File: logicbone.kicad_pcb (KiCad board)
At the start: 8 copper layers, 86.4 x 54.6 mm, 278 parts, among them IC1 ECP5UM-CABGA381, IC10 W25Q128JVSIQ, IC11 FAN5362UMP, IC12 74LVC1G07, IC13 TPS51200, IC14 KSZ9031RNXCA, IC15 TC7USB40MU, IC16 NCP349, IC2 DDR3-TFBGA78, IC3 DDR3-TFBGA78, IC4 ACT8846QM460, IC5 PI6CG18401, IC6 74LVC1G02, IC7 FUSB302-QFN14, IC8 STM32FLxx-QFN48, IC9 ADC120, J1 NGFF-KEY-E, J2 GCT_USB4110_USBC, J3 ARJM11xx-502, J4 FTSH-105-DV-K, J5 Conn_02x05_Odd_Even, J6 Micro_SD_MEM2075, P8 BB_2x23, P9 BB_2x23, SW1 SW_SPST, SW2 SW_SPST, Y1 25MHz, Y2 32.768kHz

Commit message: Replace PMIC with MXL7704, switch to SPI master programming.
The Quorvo PMIC in the original design appears to have been deprecated
on DigiKey. Out of concern for availability, let's switch to the MXL7704
instead.

In an effort to support to an FPGA-based bootloader solution, we have
switched to using SPI master mode for the ECP5 configuration data. In
the long run this might allow a considerable downsizing of the STM32.
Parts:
- removed C168, C169, C172: 10uF, Capacitor_SMD:C_0603_1608Metric
- removed C470: 1nF, Capacitor_SMD:C_0402_1005Metric
- removed D1: LED_ARGB, KiCAD_Magic:LTST-C19HE1WT
- removed R10: 47k, Resistor_SMD:R_0402_1005Metric
- removed R14: 4.7k, Resistor_SMD:R_0402_1005Metric
- removed R15: 470, Resistor_SMD:R_0402_1005Metric
- removed R32, R33: 10k, Resistor_SMD:R_0402_1005Metric
- removed RN11: 4.7k, Resistor_SMD:R_Array_Concave_4x0603
- added FB1: MPZ1608S600, Inductor_SMD:L_0603_1608Metric, B.Cu at (157.6, 86.5)
- added IC17: NCP110AMX110, Package_DFN_QFN:UDFN-4-1EP_1x1mm_P0.65mm_EP0.48x0.48mm, F.Cu at (164.1, 66.8)
- added IC18: NCP110AMX110, Package_DFN_QFN:UDFN-4-1EP_1x1mm_P0.65mm_EP0.48x0.48mm, F.Cu at (156.6, 66.8)
- added IC19: NCP115AMX250, Package_DFN_QFN:UDFN-4-1EP_1x1mm_P0.65mm_EP0.48x0.48mm, F.Cu at (154.8, 64.8)
- added R34: 4.7k, Resistor_SMD:R_0402_1005Metric, F.Cu at (113.0, 87.5)
- C101, C102, C103, C107, C250, C255, C440, C468, C524, C529, FB8, FB9: moved to B.Cu
- C117: value 1nF -> 10uF; footprint Capacitor_SMD:C_0402_1005Metric -> Capacitor_SMD:C_0603_1608Metric; moved to B.Cu
- C465: value 0.1uF -> 100nF
- C467: value 0.1uF -> 100nF; moved to B.Cu
- IC10: value W25Q128JVSIQ -> AT25SL128A; footprint Package_DFN_QFN:DFN-8-1EP_6x5mm_P1.27mm_EP2x2mm -> Package_DFN_QFN:DFN-8-1EP_6x5mm_P1.27mm_EP4x4mm
- IC13: value TPS51200 -> TPS51206; footprint Package_SON:VSON-10-1EP_3x3mm_P0.5mm_EP1.65x2.4mm -> Logicbone:WSON-10EP-2x2mm
- IC4: value ACT8846QM460 -> MXL7704; footprint Package_DFN_QFN:QFN-48-1EP_6x6mm_P0.4mm_EP4.3x4.3mm -> Package_DFN_QFN:QFN-32-1EP_5x5mm_P0.5mm_EP3.65x3.65mm
- R1: value 27k -> 20
- R2: value 3.3k -> 20
- RN10: value 4.7k -> 10k; footprint Resistor_SMD:R_Array_Concave_4x0603 -> KiCAD_Magic:EXBD-1206
- moved C467 305.4 mm to (150.8, 104.0), turned to 90 degrees
- moved FB5 292.8 mm to (161.5, 66.5)
- moved C468 284.8 mm to (145.1, 82.3), turned to 90 degrees
- moved C250 282.2 mm to (161.5, 68.1)
- moved FB4 279.3 mm to (161.5, 68.1)
- moved C255 268.8 mm to (161.5, 66.5)
- moved FB9 256.0 mm to (126.4, 88.0)
- moved C400 249.5 mm to (126.4, 88.0), turned to 180 degrees
- moved C410 248.2 mm to (126.4, 86.4), turned to 180 degrees
- moved C103 197.3 mm to (161.9, 81.0), turned to 180 degrees
- moved C101 197.1 mm to (154.5, 81.0), turned to 90 degrees
- moved C164 195.3 mm to (165.9, 67.3), turned to 270 degrees
- moved C102 185.2 mm to (156.5, 72.0)
- moved C167 182.6 mm to (152.9, 63.6), turned to 90 degrees
- moved C165 177.7 mm to (158.4, 67.3), turned to 270 degrees
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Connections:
- C117 pad 1: VDDR -> VADC
- C117 pad 2: Net-(C117-Pad2) -> GND
- C118 pad 1: VCC -> VCC3V3
- C158 pad 1: VCC -> VCC3V3
- C159 pad 1: VCC -> VCC3V3
- C160 pad 1: VCC -> VCC3V3
- C161 pad 1: VCC -> VCC3V3
- C162 pad 1: VCCIOA -> VCC1V8
- C163 pad 1: VCCIOA -> VCC1V8
- C164 pad 1: VCCIOA -> VCC1V8
- C165 pad 1: VCCIOA -> VCC1V8
- C201 pad 1: VCC -> VCC3V3
- C202 pad 1: VCC -> VCC3V3
- C210 pad 1: VCC -> VCC3V3
- C211 pad 1: VCC -> VCC3V3
- C212 pad 1: VCC -> VCC3V3
- C220 pad 1: VCCIOA -> VCC3V3
- C221 pad 1: VCCIOA -> VCC3V3
- C222 pad 1: VCCIOA -> VCC3V3
- C230 pad 1: VCCIOB -> VCC1V8
- C231 pad 1: VCCIOB -> VCC1V8
- C232 pad 1: VCCIOB -> VCC1V8
- C300 pad 1: VCC -> VCC3V3
- C301 pad 1: VCC -> VCC3V3
- C302 pad 1: VCC -> VCC3V3
- C303 pad 1: VCC -> VCC3V3
- C304 pad 1: VCC -> VCC3V3
- C305 pad 1: VCC -> VCC3V3
- C306 pad 1: VCC -> VCC3V3
- C307 pad 1: VCC -> VCC3V3
- C462 pad 1: VDDR -> GND
- C464 pad 1: VDDR -> /FPGA Memory/DDR3_VREF
- C464 pad 2: /FPGA Memory/DDR3_VREF -> GND
- D7 pad 1: GND -> Net-(D7-Pad1)
- D7 pad 2: Net-(D7-Pad2) -> VCC1V8
- D8 pad 1: GND -> Net-(D8-Pad1)
- D8 pad 2: Net-(D8-Pad2) -> VCC1V8
- IC1 pad B12: /Ethernet/FPGA_USB+ -> Net-(IC1-PadB12)
- IC1 pad C12: /Ethernet/FPGA_USB- -> Net-(IC1-PadC12)
- IC1 pad F10: VCC -> VCC3V3
- IC1 pad F11: VCC -> VCC3V3
- IC1 pad F12: VCC -> VCC3V3
- IC1 pad F9: VCC -> VCC3V3
- IC1 pad H14: VCCIOA -> VCC3V3
- IC1 pad H15: VCCIOA -> VCC3V3
- IC1 pad J15: VCCIOA -> VCC3V3
- IC1 pad L14: VCCIOB -> VCC1V8
- IC1 pad L15: VCCIOB -> VCC1V8
- IC1 pad M15: VCCIOB -> VCC1V8
- IC1 pad N17: /FPGA SERDES/M2_SDIO_CLK -> /FPGA SERDES/M2_COEX2
- IC1 pad P18: /FPGA SERDES/M2_COEX2 -> /FPGA SERDES/M2_COEX1
- IC1 pad R16: /FPGA SERDES/M2_RXD -> /FPGA SERDES/M2_TXD
- IC1 pad R17: /FPGA SERDES/M2_TXD -> /FPGA SERDES/M2_RXD
- IC1 pad R2: Net-(IC1-PadR2) -> /Supervisor/~FLASH_CSEL
- IC1 pad R3: Net-(IC1-PadR3) -> /Supervisor/USB_SEL
- IC1 pad R4: Net-(IC1-PadR4) -> GND
- IC1 pad T17: /FPGA SERDES/M2_COEX1 -> /FPGA SERDES/M2_SDIO_CLK
- IC1 pad T2: /Supervisor/~FPGA_CSEL -> /Exp Headers/PWR_BUTTON
- IC1 pad T4: Net-(IC1-PadR4) -> +3V3
- IC1 pad U17: /FPGA SERDES/M2_USB_DM -> /FPGA SERDES/M2_LED1
- IC1 pad U18: /FPGA SERDES/M2_USB_DP -> /FPGA SERDES/M2_LED2
- IC1 pad U2: /Supervisor/~FPGA_HOLDN -> /Supervisor/FPGA_UART_TXD
- IC1 pad U3: /Supervisor/FPGA_SCLK -> /Supervisor/FLASH_SCLK
- IC1 pad U4: Net-(IC1-PadU4) -> GND
- IC1 pad V1: /Supervisor/FPGA_UART_TXD -> /Supervisor/FPGA_UART_CLK
- IC1 pad V2: /Supervisor/FPGA_MISO -> /Supervisor/FLASH_MISO
- IC1 pad W1: /Supervisor/FPGA_UART_CLK -> /Supervisor/FLASH_D3
- IC1 pad W2: /Supervisor/FPGA_MOSI -> /Supervisor/FLASH_MOSI
- IC1 pad Y2: Net-(IC1-PadY2) -> /Supervisor/FLASH_D2
- IC10 pad 2: /Supervisor/FLASH_D1 -> /Supervisor/FLASH_MISO
- IC10 pad 5: /Supervisor/FLASH_D0 -> /Supervisor/FLASH_MOSI
- IC12 pad 5: VCC -> VCC3V3
- IC13 pad 1: Net-(C470-Pad2) -> VDDR
- IC13 pad 10: VCC -> VCC3V3
- IC14 pad 1: VCC -> VCC3V3
- IC14 pad 12: VCC -> VCC3V3
- IC14 pad 16: VCC -> VCC3V3
- IC14 pad 34: VCC -> VCC3V3
- IC14 pad 40: VCC -> VCC3V3
- IC4 pad 1: Net-(IC4-Pad1) -> +3V3
- IC4 pad 12: Net-(IC4-Pad11) -> VBUS
- IC4 pad 14: VBUS -> Net-(IC4-Pad14)
- IC4 pad 15: VCC -> Net-(IC4-Pad14)
- IC4 pad 16: /Supervisor/PMIC_ENABLE -> Net-(IC4-Pad14)
- IC4 pad 17: Net-(C107-Pad1) -> GND
- IC4 pad 18: VBUS -> GND
- IC4 pad 19: Net-(IC4-Pad19) -> VCORE
- IC4 pad 2: Net-(IC4-Pad1) -> /Supervisor/PMIC_SDA
- IC4 pad 20: GND -> Net-(IC4-Pad20)
- IC4 pad 21: VCCIOA -> Net-(IC4-Pad21)
- IC4 pad 22: VADC -> Net-(IC4-Pad22)
- IC4 pad 23: /Supervisor/PMIC_SCL -> GND
- IC4 pad 24: /Supervisor/PMIC_SDA -> Net-(C107-Pad1)
- IC4 pad 25: VBUS -> VCC3V3
- IC4 pad 26: Net-(IC4-Pad26) -> GND
- IC4 pad 27: GND -> Net-(IC4-Pad27)
- IC4 pad 28: Net-(IC4-Pad28) -> VBUS
- IC4 pad 29: Net-(C117-Pad2) -> VBUS
- IC4 pad 3: GND -> /Supervisor/PMIC_SCL
- IC4 pad 30: VBUS -> Net-(IC4-Pad30)
- IC4 pad 31: /Supervisor/~PMIC_PBIN -> Net-(C107-Pad1)
- IC4 pad 32: /Supervisor/PMIC_PWRHOLD -> VDDR
- IC4 pad 33: /Ethernet/~SYS_RESET -> GND
- IC4 pad 4: VCCTRX -> /Supervisor/PMIC_SEQ
- IC4 pad 5: VCCIOB -> /Ethernet/~SYS_RESET
- IC4 pad 6: +3V3 -> /Supervisor/PMIC_ENABLE
- IC4 pad 7: VCCTRXA -> +3V3
- IC4 pad 8: /Supervisor/PMIC_VSELR2 -> VCCAUX
- IC4 pad 9: /Supervisor/~PMIC_PBSTAT -> VCC1V8
- IC5 pad 16: VCCIOB -> VCC1V8
- IC5 pad 21: VCCIOB -> VCC1V8
- IC5 pad 25: VCCIOB -> VCC1V8
- IC5 pad 31: VCCIOB -> VCC1V8
- IC5 pad 4: VCCIOB -> VCC1V8
- IC5 pad 5: VCC -> VCC3V3
- IC5 pad 9: VCCIOB -> VCC1V8
- IC8 pad 10: /Supervisor/~USB_INT -> /Supervisor/PMIC_ENABLE
- IC8 pad 12: /Supervisor/~FLASH_CSEL -> Net-(IC8-Pad12)
- IC8 pad 13: /Supervisor/FLASH_SCLK -> Net-(IC8-Pad13)
- IC8 pad 14: /Supervisor/PMIC_PWRHOLD -> /Supervisor/PMIC_SEQ
- IC8 pad 15: /Supervisor/PMIC_VSELR2 -> /FPGA Power/PWR_SERDES
- IC8 pad 16: /Supervisor/FLASH_D3 -> Net-(IC8-Pad16)
- IC8 pad 17: /Supervisor/FLASH_D2 -> Net-(IC8-Pad17)
- IC8 pad 18: /Supervisor/FLASH_D1 -> Net-(IC8-Pad18)
- IC8 pad 19: /Supervisor/FLASH_D0 -> Net-(IC8-Pad19)
- IC8 pad 2: /Supervisor/~PMIC_INT -> Net-(IC8-Pad2)
- IC8 pad 25: /Supervisor/~FPGA_CSEL -> /Supervisor/~FLASH_CSEL
- IC8 pad 26: /Supervisor/FPGA_SCLK -> /Supervisor/FLASH_SCLK
- IC8 pad 27: /Supervisor/FPGA_MISO -> /Supervisor/FLASH_MISO
- IC8 pad 28: /Supervisor/FPGA_MOSI -> /Supervisor/FLASH_MOSI
- IC8 pad 38: /Supervisor/~FPGA_HOLDN -> /Supervisor/~USB_INT
- IC9 pad 13: VCC -> VCC3V3
- J1 pad 2: VCC -> VCC3V3
- J1 pad 4: VCC -> VCC3V3
- J1 pad 72: VCC -> VCC3V3
- J1 pad 74: VCC -> VCC3V3
- J6 pad 4: VCC -> VCC3V3
- L1 pad 1: Net-(IC4-Pad26) -> Net-(IC4-Pad27)
- L1 pad 2: VCCIOA -> VCC3V3
- L2 pad 1: Net-(IC4-Pad1) -> Net-(IC4-Pad14)
- L3 pad 2: VCC -> VCC1V8
- L4 pad 1: Net-(IC4-Pad28) -> Net-(IC4-Pad30)
- P9 pad 3: VCC -> VCC3V3
- P9 pad 4: VCC -> VCC3V3
- R1 pad 1: GND -> Net-(IC1-PadB12)
- R1 pad 2: Net-(C117-Pad2) -> /Ethernet/FPGA_USB+
- R11 pad 1: /FPGA SERDES/M2_LED1 -> Net-(D7-Pad1)
- R11 pad 2: Net-(D7-Pad2) -> /FPGA SERDES/M2_LED1
- R12 pad 1: /FPGA SERDES/M2_LED2 -> Net-(D8-Pad1)
- R12 pad 2: Net-(D8-Pad2) -> /FPGA SERDES/M2_LED2
- R13 pad 1: VCC -> VCC3V3
- R16 pad 1: VCC -> VCC3V3
- R17 pad 1: VCC -> VCC3V3
- R18 pad 1: VCC -> VCC3V3
- R19 pad 1: VCC -> VCC3V3
- R2 pad 1: VDDR -> Net-(IC1-PadC12)
- R2 pad 2: Net-(C117-Pad2) -> /Ethernet/FPGA_USB-
- R20 pad 1: VCC -> VCC3V3
- R21 pad 1: VCC -> VCC3V3
- R26 pad 1: /Ethernet/FPGA_USB+ -> Net-(IC1-PadB12)
- R27 pad 1: VCC -> VCC3V3
- R28 pad 1: VCC -> VCC3V3
- R30 pad 2: VCC -> VCC3V3
- R31 pad 2: VCC -> VCC3V3
- R8 pad 1: VCCIOB -> VCC1V8
- RN10 pad 1: /Ethernet/MMC_DAT2 -> VCC3V3
- RN10 pad 2: /Ethernet/MMC_DAT3 -> Net-(RN10-Pad2)
- RN10 pad 4: Net-(RN10-Pad4) -> /Ethernet/MMC_DAT3
- RN10 pad 5: VCC -> /Ethernet/MMC_DAT2
- RN10 pad 6: VCC -> /Ethernet/MMC_CLK
- RN10 pad 7: VCC -> /Ethernet/MMC_DAT0
- RN10 pad 8: VCC -> /Ethernet/MMC_DAT1
- RN4 pad 5: VCCIOB -> VCC1V8
- RN4 pad 6: VCCIOB -> VCC1V8
- RN4 pad 7: VCCIOB -> VCC1V8
- RN4 pad 8: VCCIOB -> VCC1V8
- RN5 pad 3: /Supervisor/~FPGA_CSEL -> Net-(RN5-Pad3)
- RN5 pad 4: /Supervisor/~FPGA_HOLDN -> Net-(RN5-Pad4)
- RN7 pad 1: /Supervisor/~PMIC_PBSTAT -> /Supervisor/FLASH_D3
- RN7 pad 2: /Supervisor/PMIC_ENABLE -> Net-(RN7-Pad2)
- RN7 pad 3: /Supervisor/PMIC_VSELR2 -> /Supervisor/~FLASH_CSEL
- RN7 pad 4: /Supervisor/PMIC_PWRHOLD -> /Supervisor/FLASH_D2
- RN7 pad 5: VCC -> +3V3
- RN7 pad 6: GND -> +3V3
- RN8 pad 1: /Ethernet/~SYS_RESET -> /Supervisor/PMIC_SDA
- RN8 pad 3: /Supervisor/PMIC_SDA -> /Ethernet/~SYS_RESET
- RN8 pad 4: /Supervisor/~PMIC_INT -> /Supervisor/PMIC_SEQ
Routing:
- net VCC3V3: track 0.00 -> 241.3 mm, vias 0 -> 17
- net +3V3: track 27.6 -> 197.9 mm, vias 11 -> 14
- net VCC1V8: track 0.00 -> 162.6 mm, vias 0 -> 14
- net /FPGA Memory/DDR3_VREF: track 10.1 -> 137.4 mm, vias 5 -> 7
- net VCORE: track 31.1 -> 134.4 mm
- net /DDR3 Power/VDDR_CORE: track 25.5 -> 122.2 mm, vias 17 -> 18
- net GND: track 359.9 -> 446.4 mm, vias 114 -> 126
- net /Supervisor/~PMIC_INT: track 66.3 -> 0.00 mm, vias 2 -> 0
- net /Supervisor/USB_SEL: track 0.00 -> 65.1 mm, vias 0 -> 2
- net VDDR: track 17.5 -> 79.8 mm, vias 8 -> 9
- net /Supervisor/PMIC_ENABLE: track 1.05 -> 60.8 mm, vias 1 -> 2
- net /Supervisor/PMIC_SEQ: track 0.00 -> 57.8 mm, vias 0 -> 2
- net /Supervisor/PMIC_PWRHOLD: track 54.3 -> 0.00 mm, vias 2 -> 0
- net VCCAUX: track 6.30 -> 55.7 mm
- net VCC: track 46.4 -> 0.00 mm, vias 13 -> 0
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
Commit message: Add dedicated LDO for VCCAUX, and a bunch of cleanup
The MXL7704 is almost capable of booting the entire ECP5 on its own
without any help from the supervisor. So we would like to test it out
on the prototype boards. To accompish this, we need to use a dedicated
LDO for VCCAUX.

With that, I am rapidly running out of major work to do and from here
on out it's just going to be review and minor tweaks.
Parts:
- removed C153, C157, C251, C256, C263, C273: 10uF, Capacitor_SMD:C_0603_1608Metric
- removed C503: 100nF, Capacitor_SMD:C_0402_1005Metric
- removed C507: 10nF, Capacitor_SMD:C_0402_1005Metric
- removed FB6: MPZ1608S600, Inductor_SMD:L_0603_1608Metric
- removed RN12: 47, Resistor_SMD:R_Array_Concave_4x0402
- removed RN6: 470, Resistor_SMD:R_Array_Concave_4x0603
- added C120: 100nF, Capacitor_SMD:C_0402_1005Metric, B.Cu at (181.8, 67.0)
- added C121: 100nF, Capacitor_SMD:C_0402_1005Metric, B.Cu at (177.8, 67.0)
- added C122: 100nF, Capacitor_SMD:C_0402_1005Metric, B.Cu at (179.5, 66.8)
- added C123: 100nF, Capacitor_SMD:C_0402_1005Metric, B.Cu at (178.0, 72.2)
- added D1: LED_ALT, LED_SMD:LED_0603_1608Metric, F.Cu at (183.1, 86.2)
- added D6: D_Schottky_ALT, Diode_SMD:D_SOD-123F, F.Cu at (126.0, 92.4)
- added D9: LED_ALT, LED_SMD:LED_0603_1608Metric, F.Cu at (183.1, 88.0)
- added IC20: NCP115AMX250, Package_DFN_QFN:UDFN-4-1EP_1x1mm_P0.65mm_EP0.48x0.48mm, F.Cu at (128.6, 68.9)
- added Q1: Q_PMOS_GSD, Package_TO_SOT_SMD:SOT-23, F.Cu at (119.0, 56.0)
- added R10: 470, Resistor_SMD:R_0402_1005Metric, F.Cu at (178.2, 86.8)
- added R14: 47, Resistor_SMD:R_0402_1005Metric, B.Cu at (145.9, 84.3)
- added R15: 47, Resistor_SMD:R_0402_1005Metric, B.Cu at (154.4, 83.9)
- added RN11: 10k, Resistor_SMD:R_Array_Concave_4x0603, B.Cu at (133.5, 59.9)
- C104, C155, C156, C161, C304, C442, C443, C447, C460, R1, R2, R20, R21, R22, R23, R6: moved to B.Cu
- C117, C220, C254, C262, C264, C265, C266, C270, C271, C272, C280, C302, C430, C462, C467, C521: moved to F.Cu
- C469: value 0.1uF -> 100nF
- H5: value MountingHole -> MountingHole_Pad
- R16: value 10k -> 47; moved to B.Cu
- R17: value 10k -> 470
- R19: value 10k -> 4.7k
- Y2: footprint KiCAD_Magic:Crystal_4SMD_7x1.5mm -> Crystal:Crystal_SMD_3215-2Pin_3.2x1.5mm
- moved C201 335.9 mm to (161.0, 41.3)
- moved C454 315.9 mm to (134.4, 26.3)
- moved C456 312.9 mm to (131.5, 26.3)
- moved C446 311.3 mm to (134.4, 30.3)
- moved C455 309.3 mm to (131.5, 28.3)
- moved C452 309.2 mm to (134.4, 28.3)
- moved C451 306.3 mm to (137.3, 26.3)
- moved C453 305.0 mm to (131.5, 30.3)
- moved C450 303.3 mm to (131.5, 32.3)
- moved R6 299.3 mm to (181.8, 71.7), turned to 180 degrees
- moved C444 298.5 mm to (150.5, 26.6)
- moved C447 294.8 mm to (140.8, 104.6), turned to 90 degrees
- moved C412 294.1 mm to (156.9, 26.3)
- moved C445 286.2 mm to (150.5, 29.1)
- moved C420 284.9 mm to (155.0, 85.1)
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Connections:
- C108 pad 2: Net-(C108-Pad2) -> GND
- C109 pad 2: Net-(C108-Pad2) -> GND
- C162 pad 1: VCC1V8 -> VCC3V3
- FB7 pad 2: VCORE -> /Ethernet/ETH_1V2
- H5 pad 1: (no net) -> GND
- IC1 pad N1: Net-(IC1-PadN1) -> /FPGA Memory/~DDR3_RST
- IC1 pad N4: /FPGA Memory/~DDR3_RST -> Net-(IC1-PadN4)
- IC14 pad 43: Net-(IC14-Pad43) -> /Ethernet/ETH_LDO
- IC17 pad 3: /FPGA Power/PWR_SERDES -> VCC1V8
- IC18 pad 3: /FPGA Power/PWR_SERDES -> VCC1V8
- IC4 pad 20: Net-(IC4-Pad20) -> /Supervisor/PMIC_PGOOD
- IC4 pad 5: /Ethernet/~SYS_RESET -> /FPGA Power/PWR_VCCAUX
- IC4 pad 8: VCCAUX -> Net-(IC4-Pad8)
- IC5 pad 1: Net-(C108-Pad2) -> GND
- IC8 pad 14: /Supervisor/PMIC_SEQ -> Net-(IC8-Pad14)
- IC8 pad 18: Net-(IC8-Pad18) -> /Supervisor/PMIC_SEQ
- IC8 pad 19: Net-(IC8-Pad19) -> /Supervisor/PMIC_PGOOD
- P8 pad 3: VCCIOA -> Net-(P8-Pad3)
- P8 pad 4: VCCIOA -> Net-(P8-Pad4)
- P8 pad 5: VCCIOA -> Net-(P8-Pad5)
- P8 pad 6: VCCIOA -> Net-(P8-Pad6)
- R16 pad 1: VCC3V3 -> /FPGA Memory/DDR3_CK-
- R16 pad 2: /Ethernet/ETH_RXD3 -> Net-(C469-Pad1)
- R17 pad 1: VCC3V3 -> /Supervisor/FPGA_DONE
- R17 pad 2: /Ethernet/ETH_RXD2 -> +3V3
- R18 pad 1: VCC3V3 -> /FPGA Power/PWR_VCCAUX
- R18 pad 2: /Ethernet/ETH_RXD1 -> +3V3
- R19 pad 1: VCC3V3 -> +3V3
- R19 pad 2: /Ethernet/ETH_RXD0 -> /Ethernet/~SYS_RESET
- RN5 pad 1: /Exp Headers/SDA -> /Exp Headers/SCL
- RN5 pad 2: /Exp Headers/SCL -> /Exp Headers/SDA
- RN8 pad 3: /Ethernet/~SYS_RESET -> /Supervisor/PMIC_PGOOD
- Y1 pad 2: Net-(C108-Pad2) -> GND
- Y1 pad 4: Net-(C108-Pad2) -> GND
- Y2 pad 2: GND -> Net-(C106-Pad1)
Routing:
- net GND: track 446.4 -> 1270.2 mm, vias 126 -> 144
- net VCC3V3: track 241.3 -> 366.8 mm, vias 17 -> 21
- net /Supervisor/PMIC_PGOOD: track 0.00 -> 52.3 mm, vias 0 -> 3
- net /Exp Headers/PWR_BUTTON: track 76.2 -> 125.4 mm, vias 2 -> 3
- net +3V3: track 197.9 -> 243.0 mm, vias 14 -> 18
- net /FPGA Memory/DDR3_VREF: track 137.4 -> 103.9 mm
- net /Supervisor/FPGA_DONE: track 9.68 -> 43.2 mm, vias 0 -> 2
- net /Ethernet/ETH_1V2: track 17.1 -> 49.1 mm, vias 6 -> 7
- net Net-(J3-PadL1): track 0.00 -> 27.4 mm, vias 0 -> 1
- net /FPGA Memory/~DDR3_RST: track 12.6 -> 37.4 mm, vias 2 -> 3
- net /Supervisor/~FPGA_INIT: track 16.4 -> 38.4 mm, vias 2 -> 3
- net /Ethernet/ETH_LED_L: track 26.6 -> 47.8 mm
- net /FPGA Power/PWR_VCCAUX: track 0.00 -> 20.7 mm
- net /FPGA Power/PWR_SERDES: track 0.00 -> 19.8 mm, vias 0 -> 2
- net VCCIOA: track 18.4 -> 0.00 mm
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
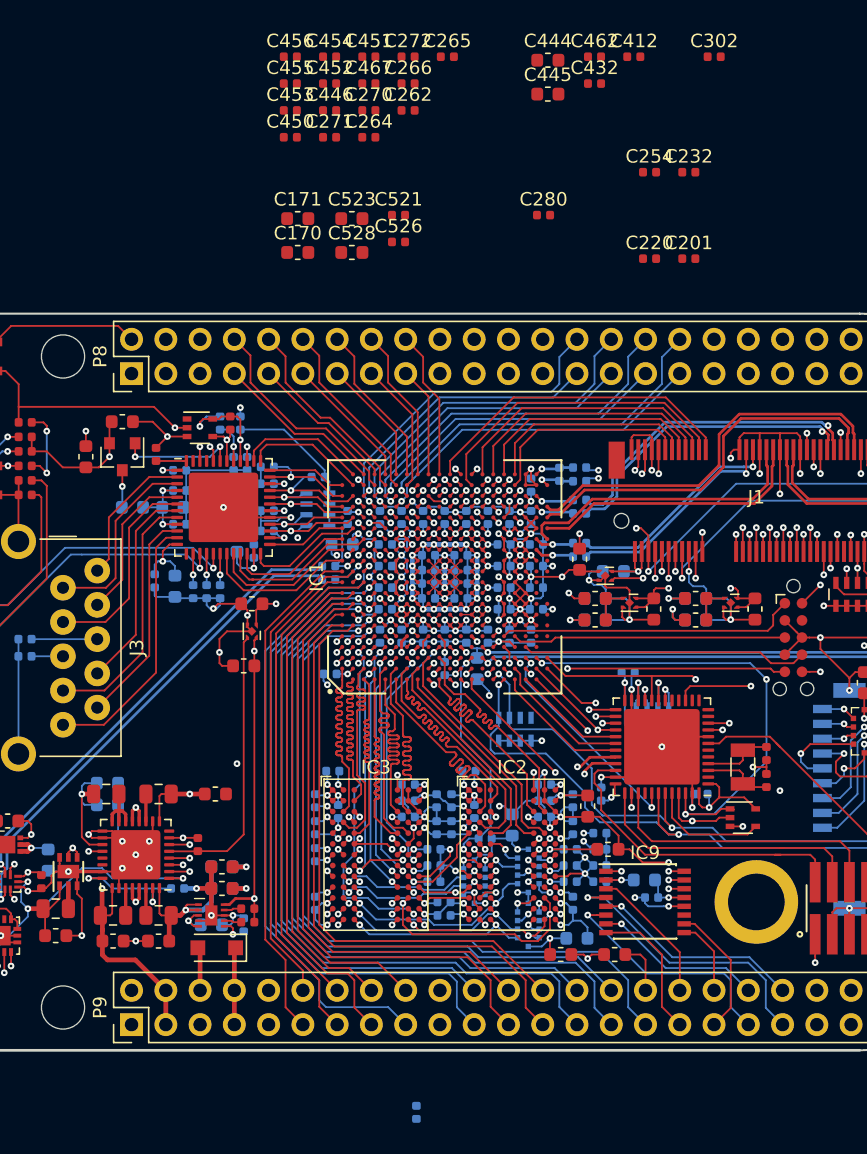
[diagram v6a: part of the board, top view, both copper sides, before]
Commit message: Place VTT bypass caps, revisit DDR length matching.
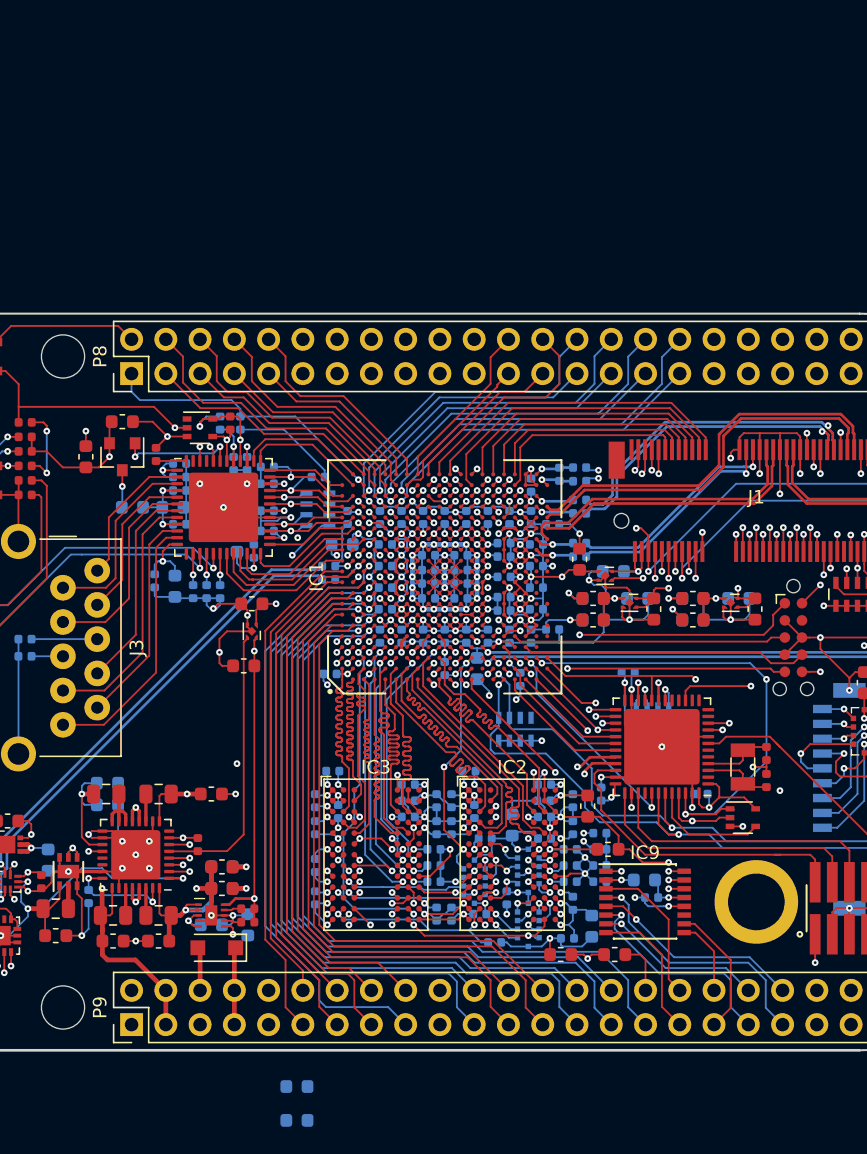
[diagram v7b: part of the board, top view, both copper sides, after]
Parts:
- removed C212, C220, C232, C262, C271, C272, C413, C433, C446, C447, C450, C453: 100nF, Capacitor_SMD:C_0402_1005Metric
- removed the C266 at (140.2, 28.3)
- removed C274, C275, C276, C466, C468: 10nF, Capacitor_SMD:C_0402_1005Metric
- removed C523, C528: 10uF, Capacitor_SMD:C_0603_1608Metric
- C170, C171, C201, C254, C280, C302, C412, C432, C444, C445, C451, C452, C454, C455, C456, C462, C467, C521, C526: moved to B.Cu
- C264, C265: value 10nF -> 100nF; moved to B.Cu
- C266: renamed from C270; moved to B.Cu
- C460: value 0.1uF -> 10uF; footprint Capacitor_SMD:C_0402_1005Metric -> Capacitor_SMD:C_0603_1608Metric
- moved C444 80.8 mm to (131.9, 105.2)
- moved C445 75.9 mm to (131.9, 102.7)
- moved C454 67.7 mm to (152.0, 91.7)
- moved C456 65.1 mm to (145.5, 89.9), turned to 180 degrees
- moved C451 63.2 mm to (147.5, 88.7), turned to 270 degrees
- moved C455 59.1 mm to (150.3, 84.3)
- moved C412 57.6 mm to (140.2, 81.5), turned to 180 degrees
- moved C452 57.1 mm to (145.9, 84.3), turned to 180 degrees
- moved C462 56.7 mm to (145.1, 82.3), turned to 270 degrees
- moved C432 53.3 mm to (150.2, 81.5), turned to 180 degrees
- moved C302 50.4 mm to (123.2, 57.5)
- moved C467 43.7 mm to (142.9, 71.7), turned to 270 degrees
- moved C265 43.0 mm to (144.5, 69.3), turned to 270 degrees
- moved C170 41.6 mm to (164.7, 66.5)
- moved C266 40.0 mm to (146.1, 69.3), turned to 270 degrees
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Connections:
- net Net-(P8-Pad22) renamed /Exp Headers/SPARE_YY
- C451 pad 1: VDDR -> VTT
- C451 pad 2: VTT -> GND
- C452 pad 1: VDDR -> VTT
- C452 pad 2: VTT -> GND
- C454 pad 1: VDDR -> VTT
- C454 pad 2: VTT -> GND
- C455 pad 1: VDDR -> VTT
- C455 pad 2: VTT -> GND
- C456 pad 1: VDDR -> VTT
- C456 pad 2: VTT -> GND
- IC1 pad D2: /FPGA Memory/~DDR3_WE -> /FPGA Memory/DDR3_A12
- IC1 pad E4: /FPGA Memory/DDR3_A12 -> /FPGA Memory/~DDR3_WE
- IC1 pad E5: /FPGA Memory/DDR3_A1 -> /FPGA Memory/DDR3_A4
- IC1 pad F4: /FPGA Memory/DDR3_A4 -> /FPGA Memory/DDR3_A1
- IC1 pad M1: /FPGA Memory/DDR3_BA2 -> /FPGA Memory/~DDR3_CAS
- IC1 pad N2: /FPGA Memory/~DDR3_CAS -> /FPGA Memory/DDR3_BA2
- P8 pad 10: /Exp Headers/P8_LVDS2n -> /Exp Headers/P8_LVDS4n
- P8 pad 11: /Exp Headers/P8_LVDS3p -> Net-(P8-Pad11)
- P8 pad 12: /Exp Headers/P8_LVDS3n -> Net-(P8-Pad12)
- P8 pad 13: /Exp Headers/P8_LVDS4p -> Net-(P8-Pad13)
- P8 pad 14: /Exp Headers/P8_LVDS4n -> Net-(P8-Pad14)
- P8 pad 15: /Exp Headers/P8_LVDS5p -> Net-(P8-Pad15)
- P8 pad 16: /Exp Headers/P8_LVDS5n -> Net-(P8-Pad16)
- P8 pad 17: /Exp Headers/P8_LVDS6p -> Net-(P8-Pad17)
- P8 pad 18: /Exp Headers/P8_LVDS6n -> /Exp Headers/SPARE_XX
- P8 pad 23: Net-(P8-Pad23) -> /Exp Headers/P8_LVDS5p
- P8 pad 24: Net-(P8-Pad24) -> /Exp Headers/P8_LVDS5n
- P8 pad 25: Net-(P8-Pad25) -> /Exp Headers/P8_LVDS6p
- P8 pad 26: Net-(P8-Pad26) -> /Exp Headers/P8_LVDS6n
- P8 pad 3: Net-(P8-Pad3) -> /Exp Headers/P8_LVDS1p
- P8 pad 4: Net-(P8-Pad4) -> /Exp Headers/P8_LVDS1n
- P8 pad 5: Net-(P8-Pad5) -> /Exp Headers/P8_LVDS2p
- P8 pad 6: Net-(P8-Pad6) -> /Exp Headers/P8_LVDS2n
- P8 pad 7: /Exp Headers/P8_LVDS1p -> /Exp Headers/P8_LVDS3p
- P8 pad 8: /Exp Headers/P8_LVDS1n -> /Exp Headers/P8_LVDS3n
- P8 pad 9: /Exp Headers/P8_LVDS2p -> /Exp Headers/P8_LVDS4p
- R14 pad 2: /FPGA Memory/DDR3_ODT0 -> /FPGA Memory/DDR3_A7
- RN3 pad 4: /FPGA Memory/DDR3_BA2 -> /FPGA Memory/~DDR3_CAS
- RN3 pad 5: /FPGA Memory/~DDR3_CAS -> /FPGA Memory/DDR3_BA2
- RN3 pad 6: /FPGA Memory/~DDR3_CS -> /FPGA Memory/DDR3_ODT0
- RN3 pad 7: /FPGA Memory/DDR3_BA0 -> /FPGA Memory/~DDR3_CS
- RN3 pad 8: /FPGA Memory/DDR3_A3 -> /FPGA Memory/DDR3_BA0
- RN3 pad 9: /FPGA Memory/DDR3_A7 -> /FPGA Memory/DDR3_A3
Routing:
- net GND: track 1270.2 -> 1315.7 mm, vias 144 -> 146
- net VTT: track 58.2 -> 64.6 mm
- net /FPGA Power/VCCA0: track 10.8 -> 16.4 mm
- net /FPGA Power/VCCA1: track 11.8 -> 17.1 mm
- net VCC3V3: track 366.8 -> 371.9 mm, vias 21 -> 22
- net /Exp Headers/P8_LVDS1p: track 12.7 -> 17.8 mm
- net /Exp Headers/P8_LVDS2p: track 11.2 -> 16.3 mm
- net /Exp Headers/P8_LVDS1n: track 16.4 -> 21.4 mm
- net /Exp Headers/P8_LVDS2n: track 14.8 -> 19.8 mm
- net /Exp Headers/P8_LVDS6n: track 11.0 -> 16.0 mm
- net /Exp Headers/P8_LVDS3p: track 10.00 -> 14.7 mm
- net /Exp Headers/P8_LVDS3n: track 13.7 -> 18.3 mm
- net /Exp Headers/P8_LVDS4n: track 12.1 -> 16.1 mm
- net /Exp Headers/P8_LVDS4p: track 9.28 -> 13.3 mm
- net /Exp Headers/P8_LVDS6p: track 8.17 -> 12.0 mm
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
